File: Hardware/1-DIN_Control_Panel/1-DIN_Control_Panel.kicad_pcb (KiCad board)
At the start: 2 copper layers, 374.9 x 296.6 mm, 76 parts, among them J1 Selector Knob Connector, J10 2x05 Molex Micro-Fit 3.0 43045, J11 2x05 Molex Micro-Fit 3.0 43045, J12 Display LEDs, J13 Mode LEDs, J2 Rotary Switch 1x7, J3 2x05 Molex Micro-Fit 3.0 43045, J4 UART Expansion, J5 SW - Aux Jump-Start, J6 SW - Battery Bypass, J7 SW - Master Power, J8 Pot/SW - Brightness, J9 2x05 Molex Micro-Fit 3.0 43045, K1 FINDER-40.52, U1 XZFAVG10, U10 XZFAVG10, U11 MAX 6954 - SSOP, U12 LM324DR, U13 12V->5V Variable Boost Buck C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, U2 XZFAVG10, U3 XZFAVG10, U4 XZFAVG10, U5 LTV-847S, U6 LTV-847S, U7 XZFAVG10, U8 XZFAVG10, U9 XZFAVG10

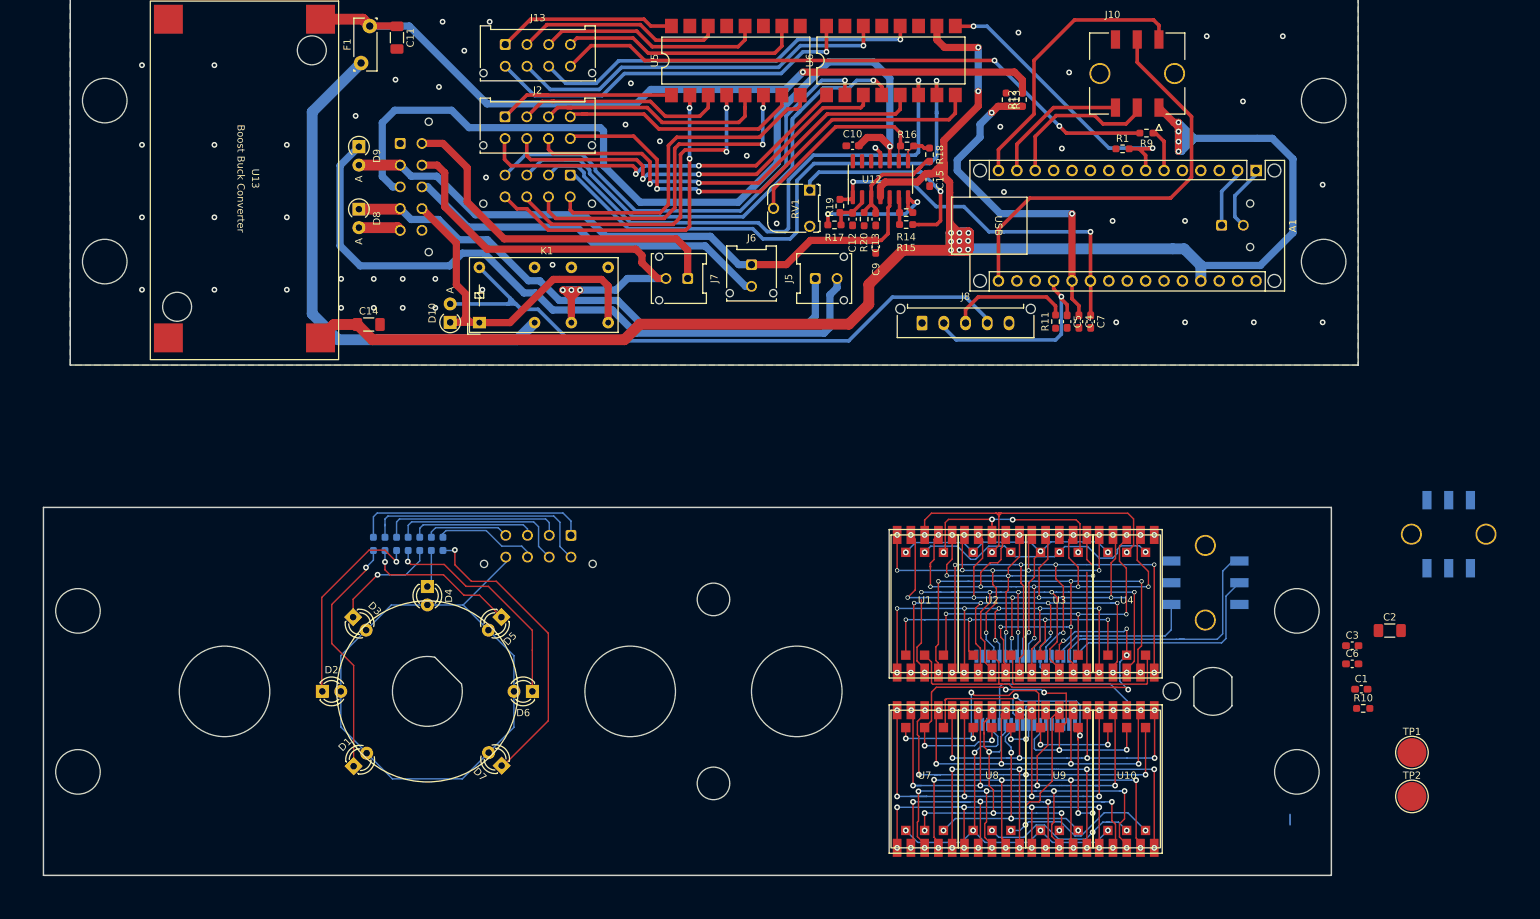
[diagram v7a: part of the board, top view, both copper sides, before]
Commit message: Most of top board is routed
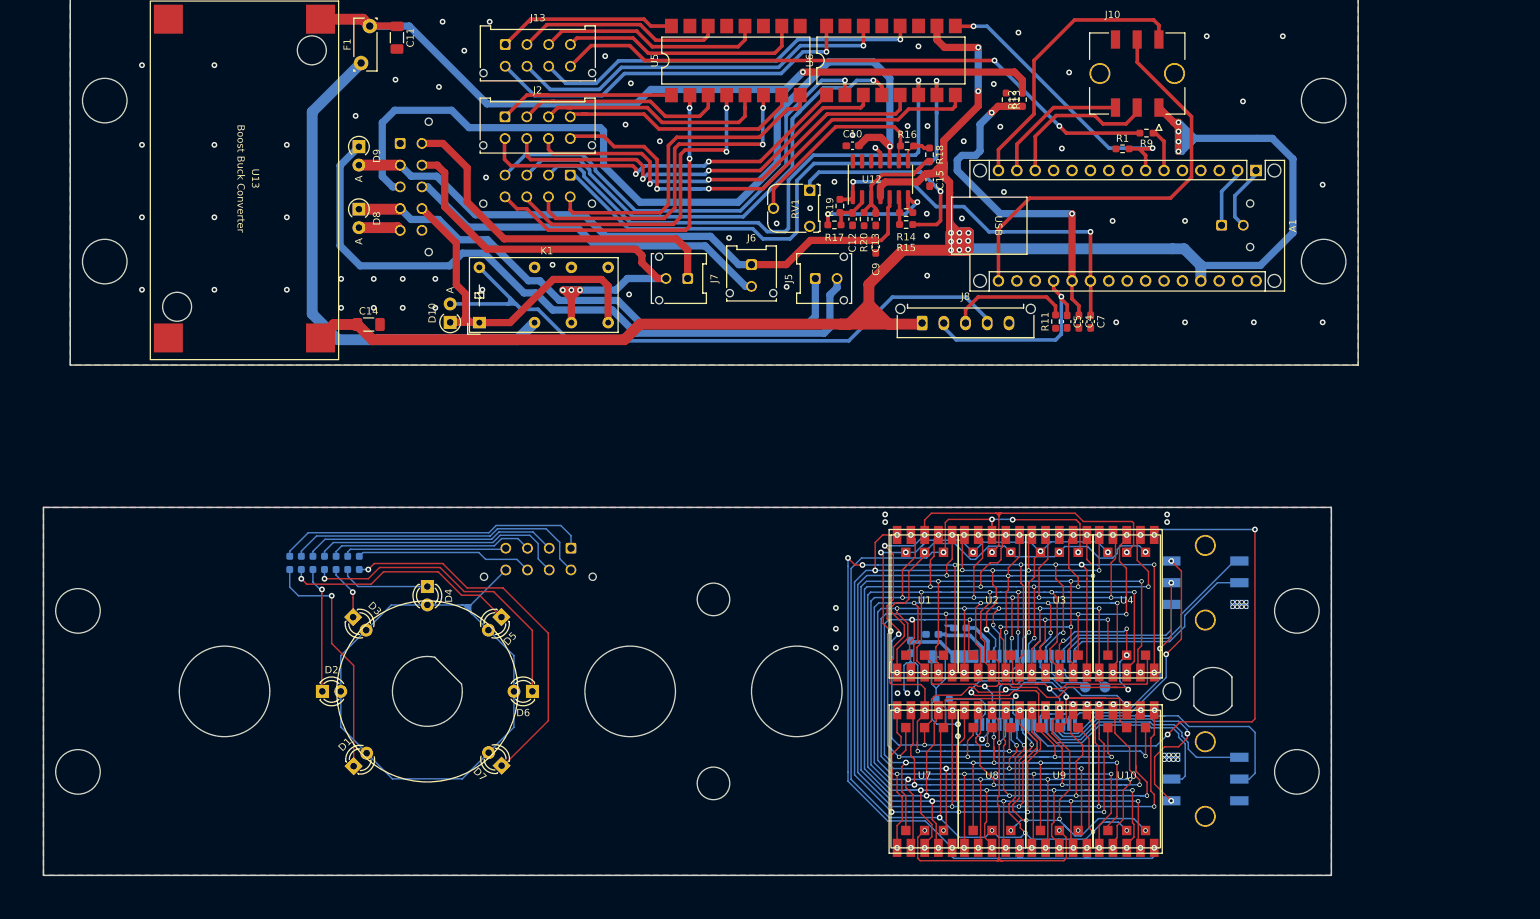
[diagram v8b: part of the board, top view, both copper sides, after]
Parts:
- C1, C2, C3, C6, R10: moved to B.Cu
- TP1, TP2: footprint TestPoint:TestPoint_Pad_D4.0mm -> TestPoint:TestPoint_Pad_D1.5mm; moved to B.Cu
- moved C2 61.7 mm to (142.7, 130.2), turned to 180 degrees
- moved C6 61.0 mm to (138.1, 128.8), turned to -90 degrees
- moved C1 59.7 mm to (141.1, 127.1), turned to 180 degrees
- moved R10 58.1 mm to (142.6, 136.0)
- moved C3 54.2 mm to (144.9, 126.2), turned to 180 degrees
- moved J9 47.7 mm to (178.8, 147.1), turned to -90 degrees
- moved TP1 46.0 mm to (162.2, 134.3)
- moved TP2 45.0 mm to (164.9, 134.3), turned to 180 degrees
- moved R3 11.8 mm to (55.6, 117.2)
- moved R2 11.8 mm to (52.4, 117.2)
- moved R5 11.8 mm to (60.4, 117.2)
- moved R6 11.8 mm to (54.0, 117.2)
- moved R7 11.8 mm to (57.2, 117.2)
- moved R8 11.8 mm to (62.0, 117.2)
- moved R4 11.8 mm to (58.8, 117.2)
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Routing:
- net /Front Board/6954_O1: track 0.00 -> 87.6 mm, vias 1 -> 3
- net /Front Board/6954_O11: track 105.9 -> 188.7 mm
- net /Front Board/6954_O4: track 105.8 -> 181.0 mm
- net /Front Board/6954_O15: track 134.8 -> 203.2 mm
- net /Front Board/6954_O8: track 97.7 -> 165.1 mm, vias 9 -> 11
- net /Front Board/6954_O14: track 94.2 -> 154.5 mm, vias 10 -> 12
- net /Front Board/6954_O9: track 139.8 -> 193.4 mm, vias 17 -> 18
- net /Front Board/6954_O17: track 127.0 -> 177.9 mm
- net /Front Board/6954_O10: track 122.8 -> 172.4 mm
- net +5V: track 289.5 -> 338.2 mm
- net /Front Board/6954_O5: track 81.8 -> 129.9 mm, vias 8 -> 10
- net /Front Board/6954_O13: track 149.0 -> 195.0 mm
- net GND: track 2.16 -> 44.6 mm, vias 49 -> 93
- net /Front Board/6954_O0: track 109.6 -> 151.9 mm
- net /Front Board/6954_O12: track 149.9 -> 191.3 mm
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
